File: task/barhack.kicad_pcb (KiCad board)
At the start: 2 copper layers, 121.9 x 49.5 mm, 89 parts, among them IC1 SIM900, J1 5V DC, J10 SWD, J2 SIMHOLDER, J3 U.FL, J4 IO, J5 BOOT0, J6 BOOT0, J7 EX1, J8 ACCEPTOR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

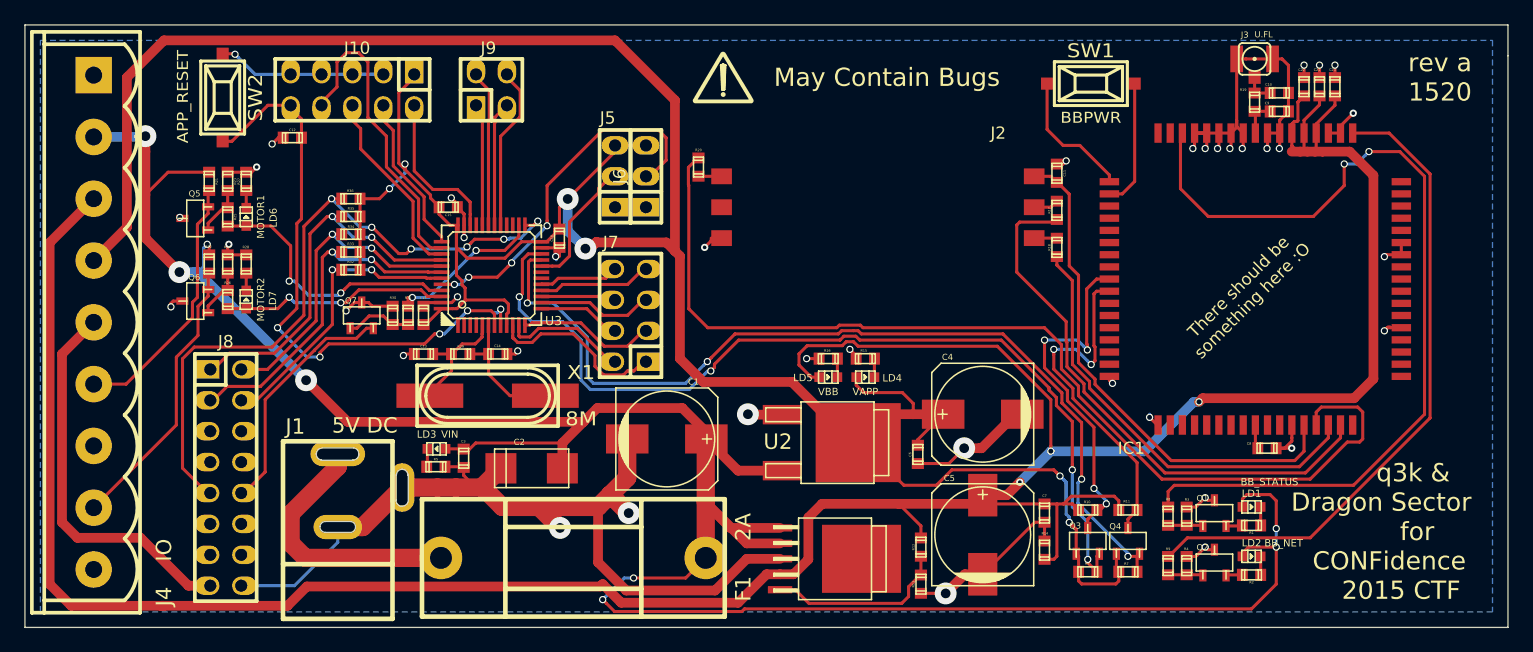
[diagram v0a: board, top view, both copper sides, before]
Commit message: Change via physical sizes (to increase copper surface), resend to Satland.
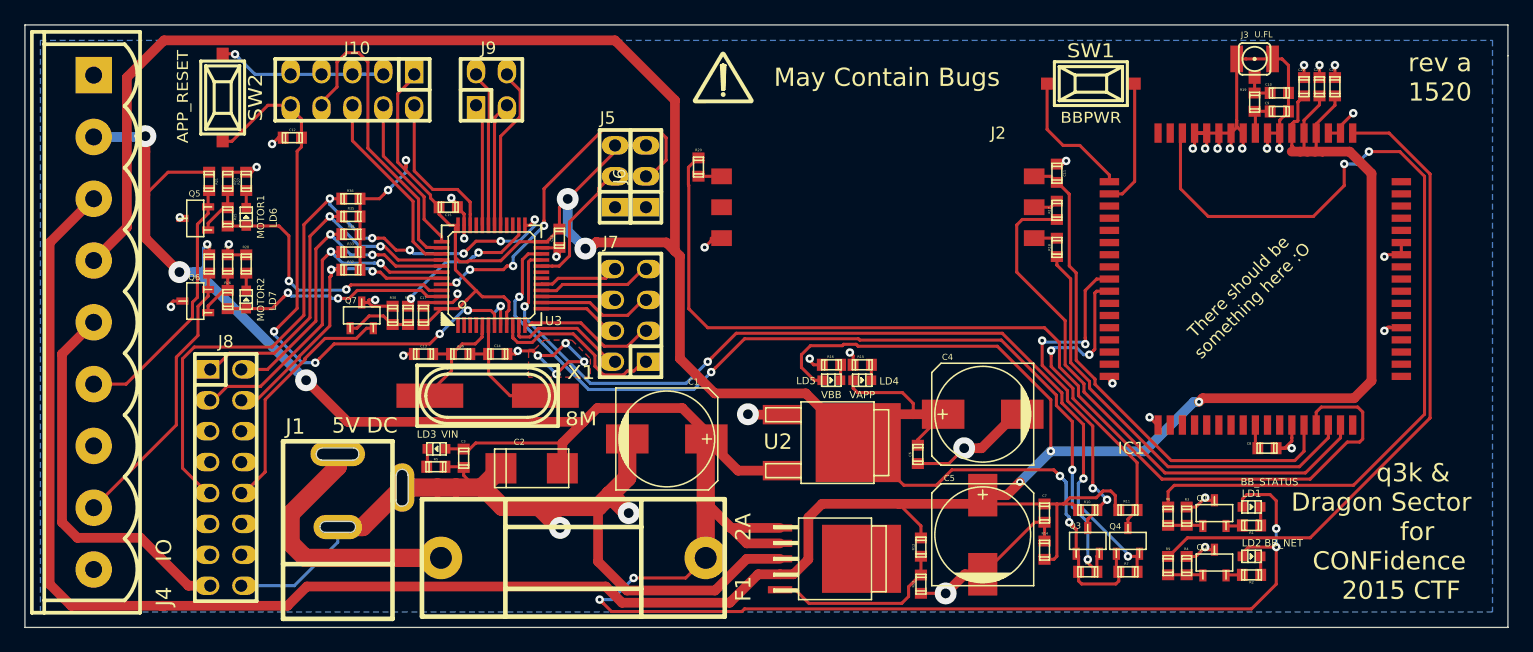
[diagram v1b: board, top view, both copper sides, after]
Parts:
- moved R16 0.57 mm to (129.8, 114.3)
- moved R15 0.57 mm to (132.3, 114.3)
- moved LD5 0.36 mm to (129.8, 115.6)
- moved LD4 0.36 mm to (132.3, 115.6)
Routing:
- net GND: track 207.9 -> 220.0 mm, vias 41 -> 45
- net 3V3: track 236.4 -> 238.5 mm
- net /BB_TX: track 76.2 -> 74.7 mm
- net /BB_RX: track 75.6 -> 74.6 mm
- net Net-(IC1-Pad10): track 28.8 -> 27.8 mm
- net /APP_RST: track 47.9 -> 48.9 mm
- net Net-(IC1-Pad9): track 29.4 -> 28.9 mm
- net +5V: track 202.9 -> 203.4 mm
- added copper zone on F.Cu, net GND
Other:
- net class Default: via_dia 0.6 -> 0.7; via_drill 0.4 -> 0.3
- board text removed: "Internet of Booze"
